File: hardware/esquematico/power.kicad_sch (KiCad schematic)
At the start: 16 parts, among them IC1 AP2112K-3.3TRG1, U1 TPSM33615FRDNR, U6 TPSM84209RKHR

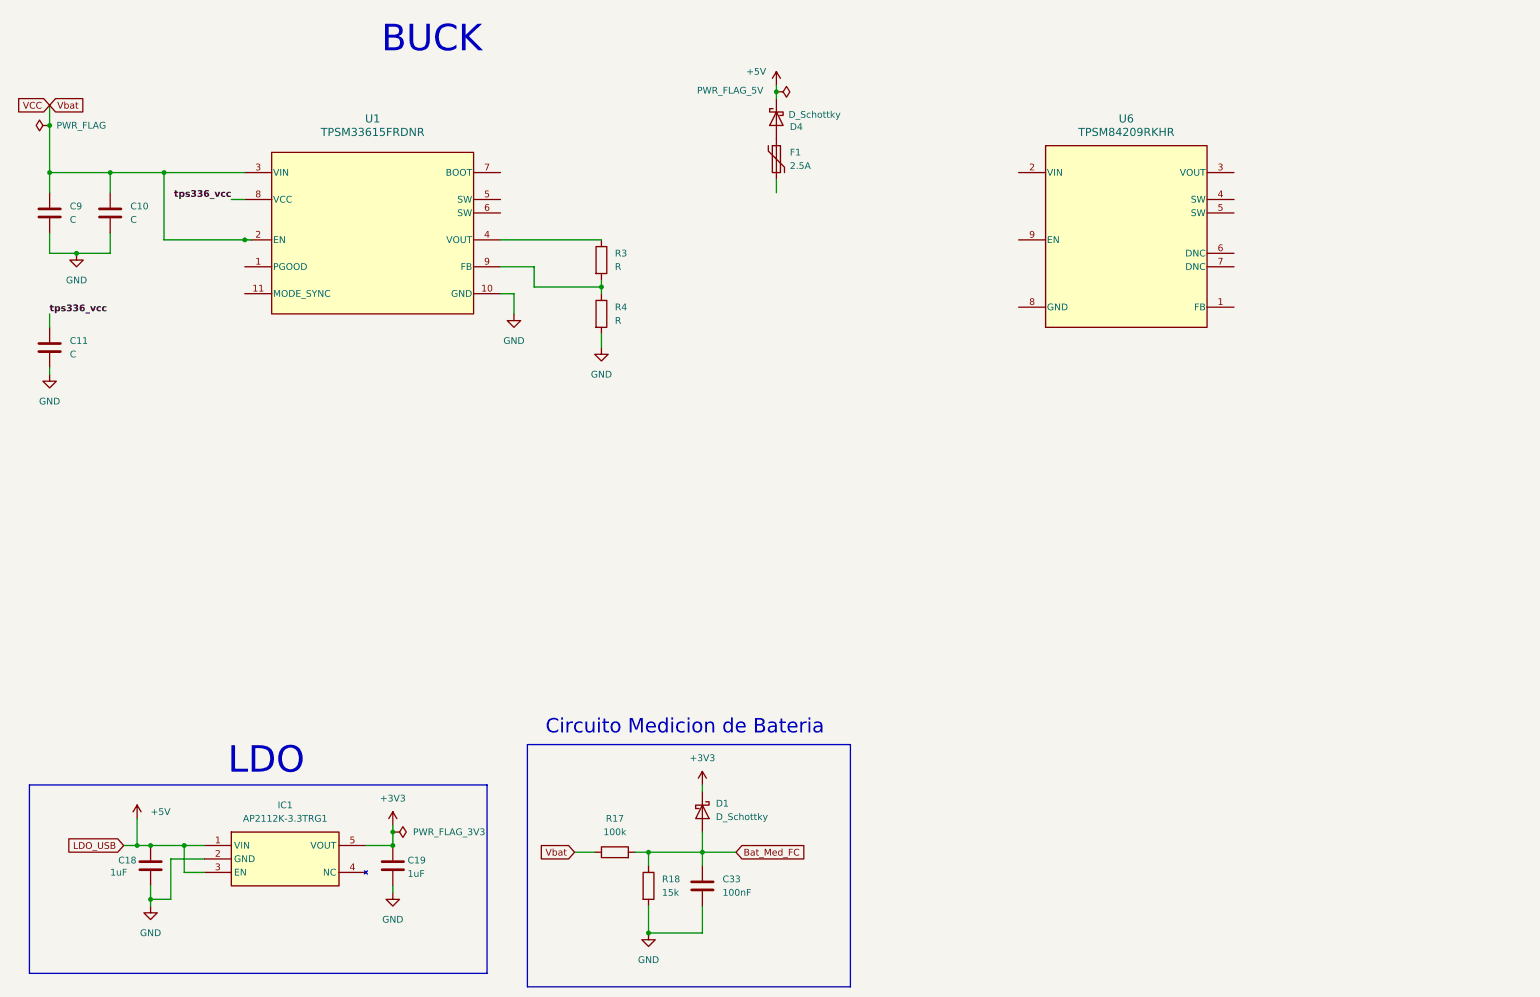
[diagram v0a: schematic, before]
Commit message: chore(hardware): restore main PCB (SDIO microSD) to match current .ioc
The new PCB (W25Q128 SPI flash, TPSM bucks) now lives in the NewPCB branch.

Co-authored-by: Cursor <cursoragent@cursor.com>
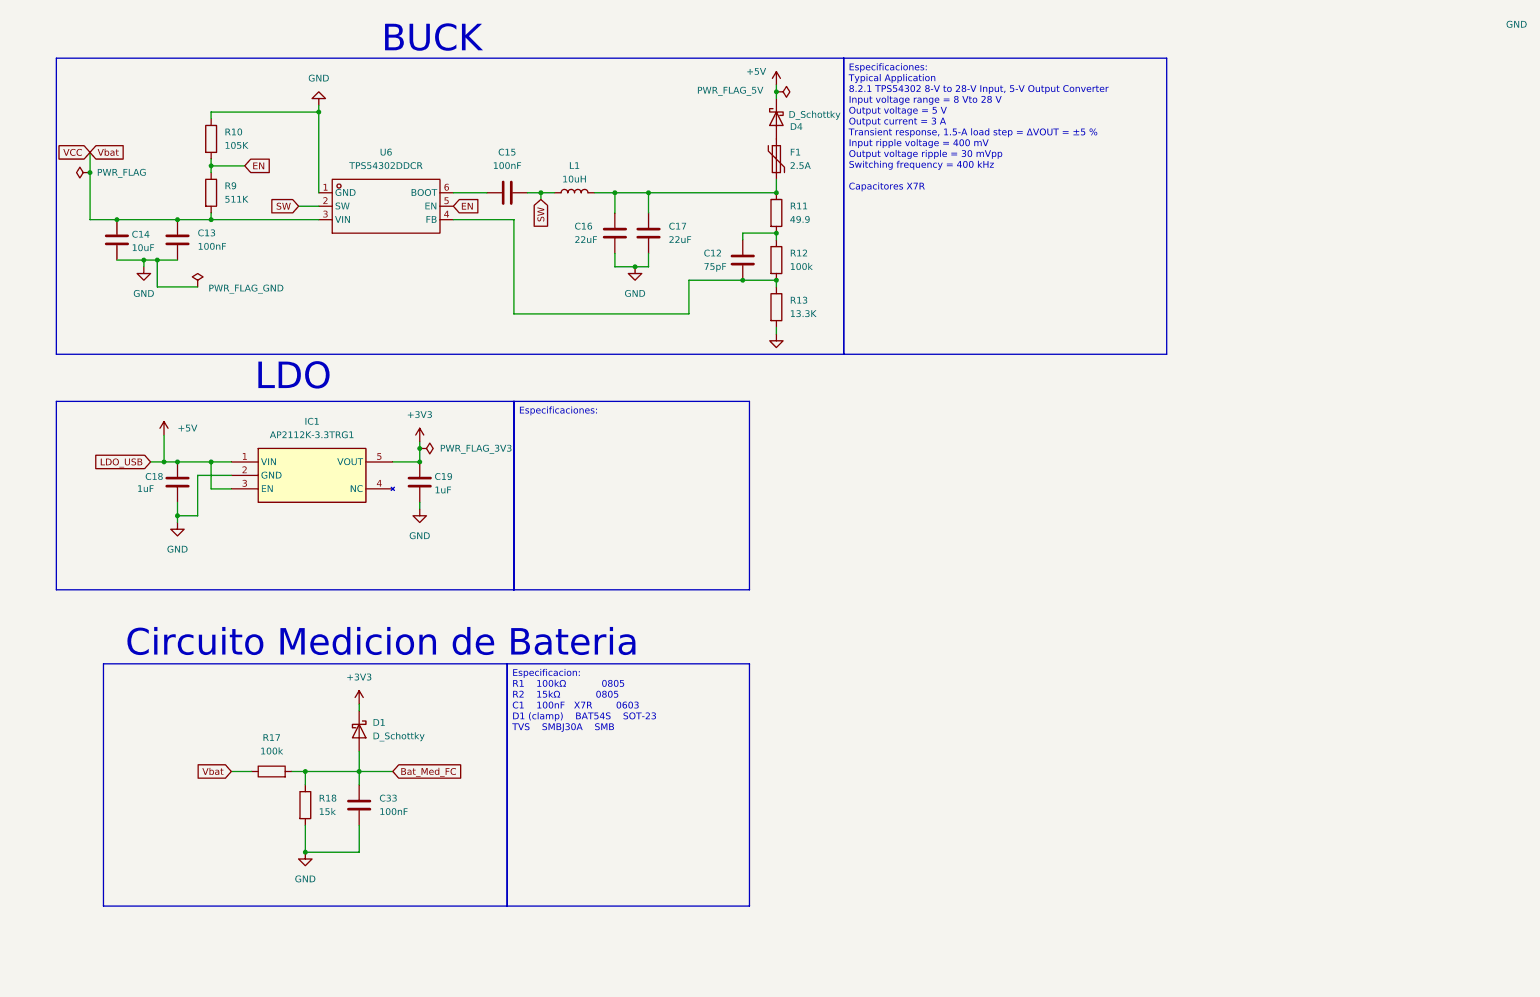
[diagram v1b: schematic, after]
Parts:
- removed C10, C11, C9: C, symbol Device:C
- removed R3, R4: R, symbol Device:R
- removed U1: TPSM33615FRDNR, RDN0011A-MFG, symbol TPSM33615FRDNR:TPSM33615FRDNR
- removed U6: TPSM84209RKHR, RKH0009A, symbol TPSM84209RKHR:TPSM84209RKHR
- added C12: 75pF, Capacitor_SMD:C_0805_2012Metric_Pad1.18x1.45mm_HandSolder, symbol Device:C
- added C13, C15: 100nF, Capacitor_SMD:C_0805_2012Metric_Pad1.18x1.45mm_HandSolder, symbol Device:C
- added C14: 10uF, Capacitor_SMD:C_0805_2012Metric_Pad1.18x1.45mm_HandSolder, symbol Device:C
- added C16, C17: 22uF, Capacitor_SMD:C_0805_2012Metric_Pad1.18x1.45mm_HandSolder, symbol Device:C
- added L1: 10uH, Inductor_SMD:L_KOHERelec_MDA7030, symbol Device:L
- added R10: 105K, Resistor_SMD:R_0805_2012Metric_Pad1.20x1.40mm_HandSolder, symbol Device:R
- added R11: 49.9, Resistor_SMD:R_0805_2012Metric_Pad1.20x1.40mm_HandSolder, symbol Device:R
- added R12: 100k, Resistor_SMD:R_0805_2012Metric_Pad1.20x1.40mm_HandSolder, symbol Device:R
- added R13: 13.3K, Resistor_SMD:R_0805_2012Metric_Pad1.20x1.40mm_HandSolder, symbol Device:R
- added R9: 511K, Resistor_SMD:R_0805_2012Metric_Pad1.20x1.40mm_HandSolder, symbol Device:R
- added U6: TPS54302DDCR, TPS54302DDCR:SOT-23-6_L2.9-W1.6-P0.95-LS2.8-BL, symbol TPS54302DDCR:TPS54302DDCR_C311983
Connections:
- net GND: now also C13.1, C14.1, C16.1, C17.1, R10.1, R13.2, U6.1 (GND)
- net VCC: now also C13.2, C14.2, R9.2, U6.3 (VIN)
- net at F1.2: now also C16.2, C17.2, L1.2, R11.1
- new net: C12.1, R11.2, R12.1
- new net: C12.2, R12.2, R13.1, U6.4 (FB)
- new net: C15.1, U6.6 (BOOT)
- new net EN: R10.2, R9.1, U6.5 (EN)
- new net SW: C15.2, L1.1, U6.2 (SW)
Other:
- moved on the sheet: C18, C19, C33, D1, IC1, R17, R18
